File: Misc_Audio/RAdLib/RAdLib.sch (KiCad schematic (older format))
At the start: 45 parts, among them J5 AudioJack3, Q1 2N3904, U1 YM3812, U2 YM3014B, U3 RC4136, U4 LM386, X1 ECS-2100AX-3.579545MHZ

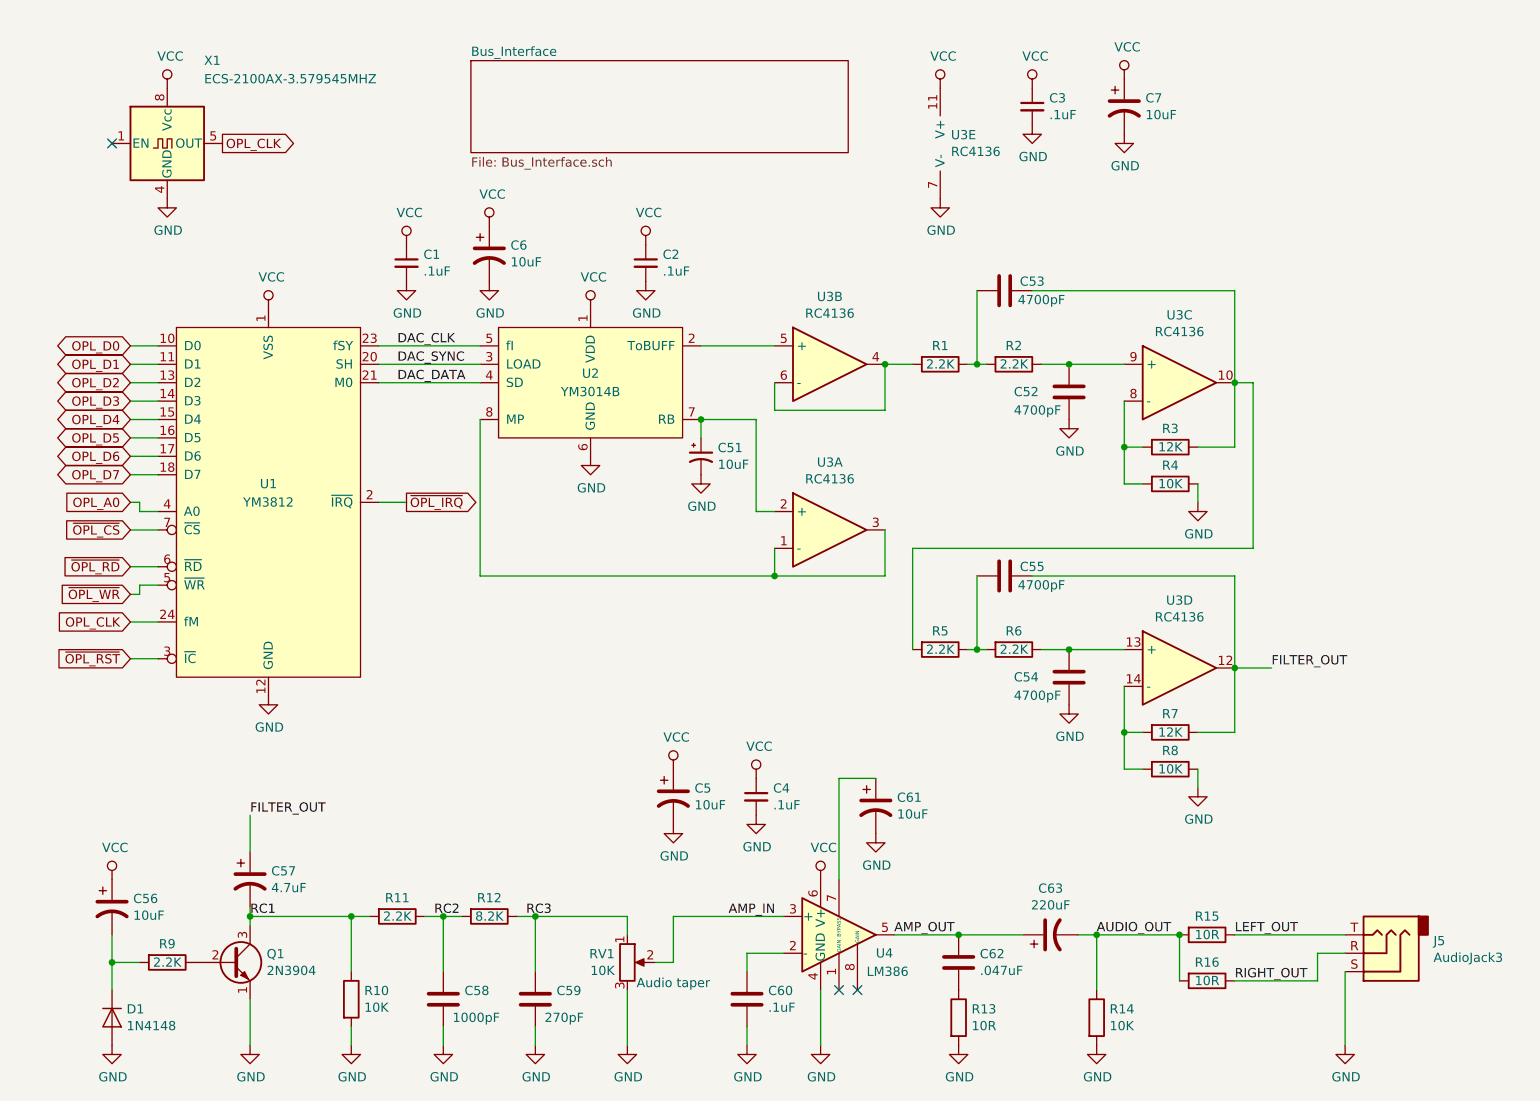
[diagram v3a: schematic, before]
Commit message: Update the active filter stages after the DAC to work with the power supply constraints on the RPI.  Document what needs to be done to the audio output section.
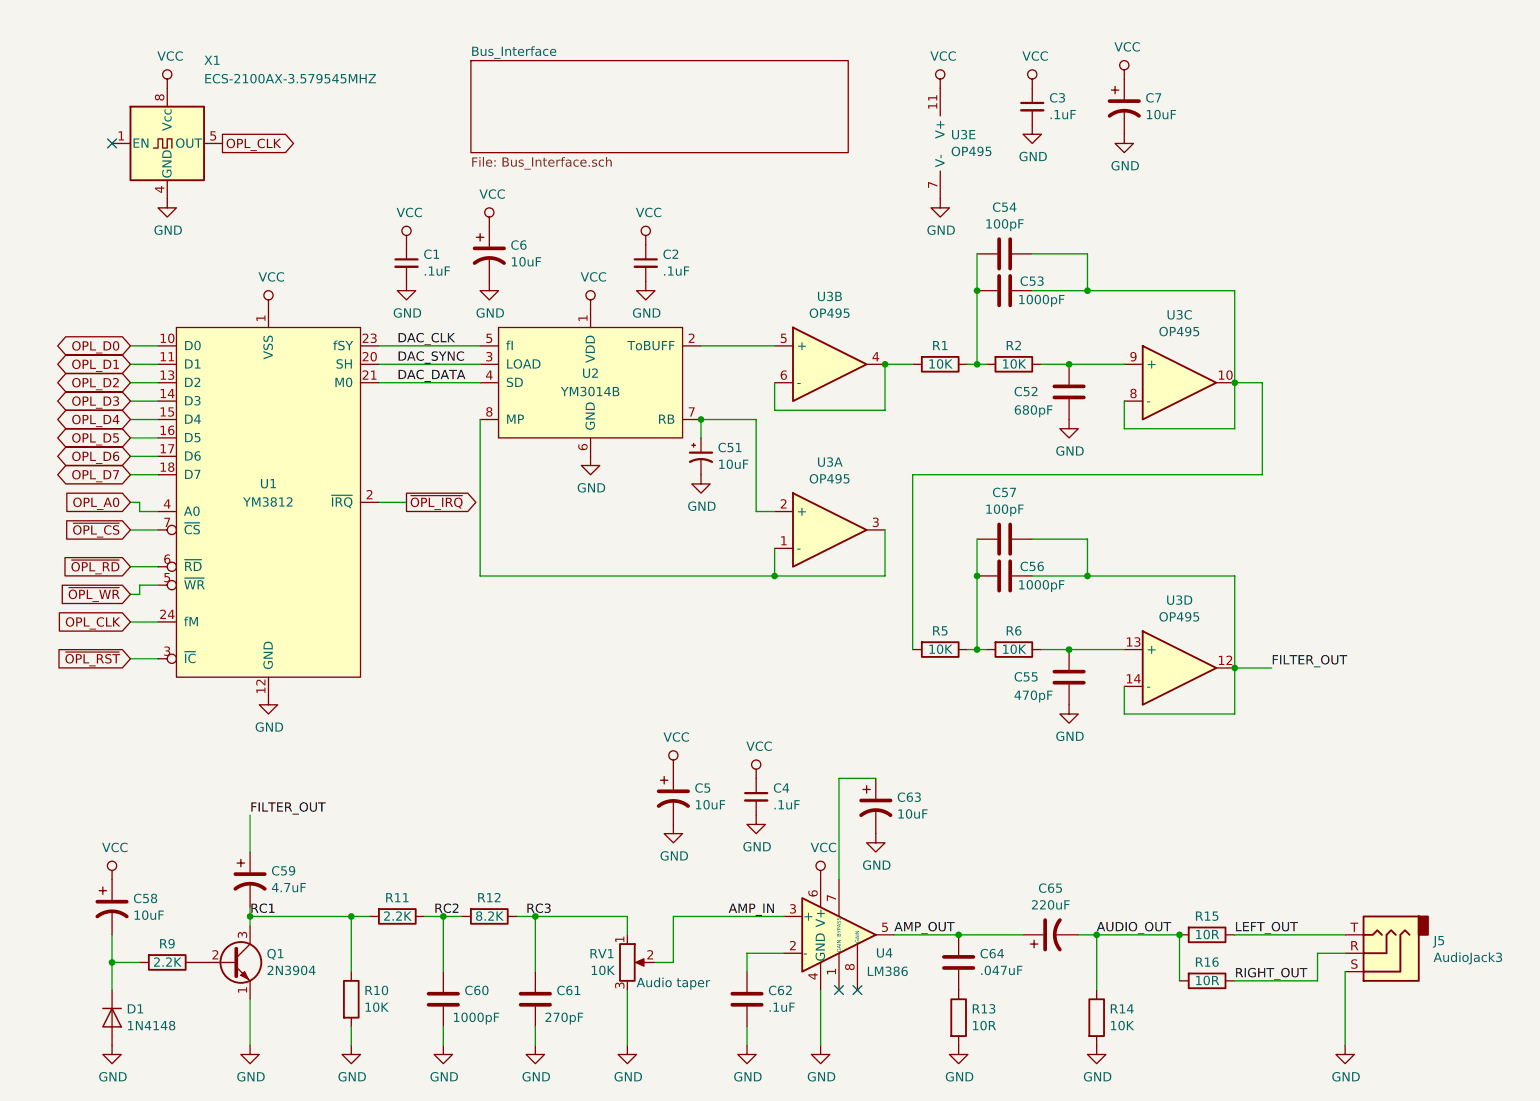
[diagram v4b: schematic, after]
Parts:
- removed R3, R7: 12K, Resistor_THT:R_Axial_DIN0204_L3.6mm_D1.6mm_P5.08mm_Horizontal, symbol Device:R
- removed R4, R8: 10K, Resistor_THT:R_Axial_DIN0204_L3.6mm_D1.6mm_P5.08mm_Horizontal, symbol Device:R
- added C54, C57: 100pF, symbol Device:C
- C52: value 4700pF -> 680pF
- C53: value 4700pF -> 1000pF
- C55: renamed from C54; value 4700pF -> 470pF
- C56: renamed from C55; value 4700pF -> 1000pF
- R1, R2, R5, R6: value 2.2K -> 10K
- U3: value RC4136 -> OP495
- renumbered C56 to C58, C57 to C59, C58 to C60, C59 to C61, C60 to C62, C61 to C63, C62 to C64, C63 to C65
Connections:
- net FILTER_OUT: now also U3.14 (-), C57.1
- net at C53.2, R1.1, R2.2: now also C54.2
- net at C53.1, R5.2, U3.10: now also U3.8 (-), C54.1
- net at C56.2, R5.1, R6.2: now also C57.2

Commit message: Rework the audio output section as an AC-coupled emitter-follower.
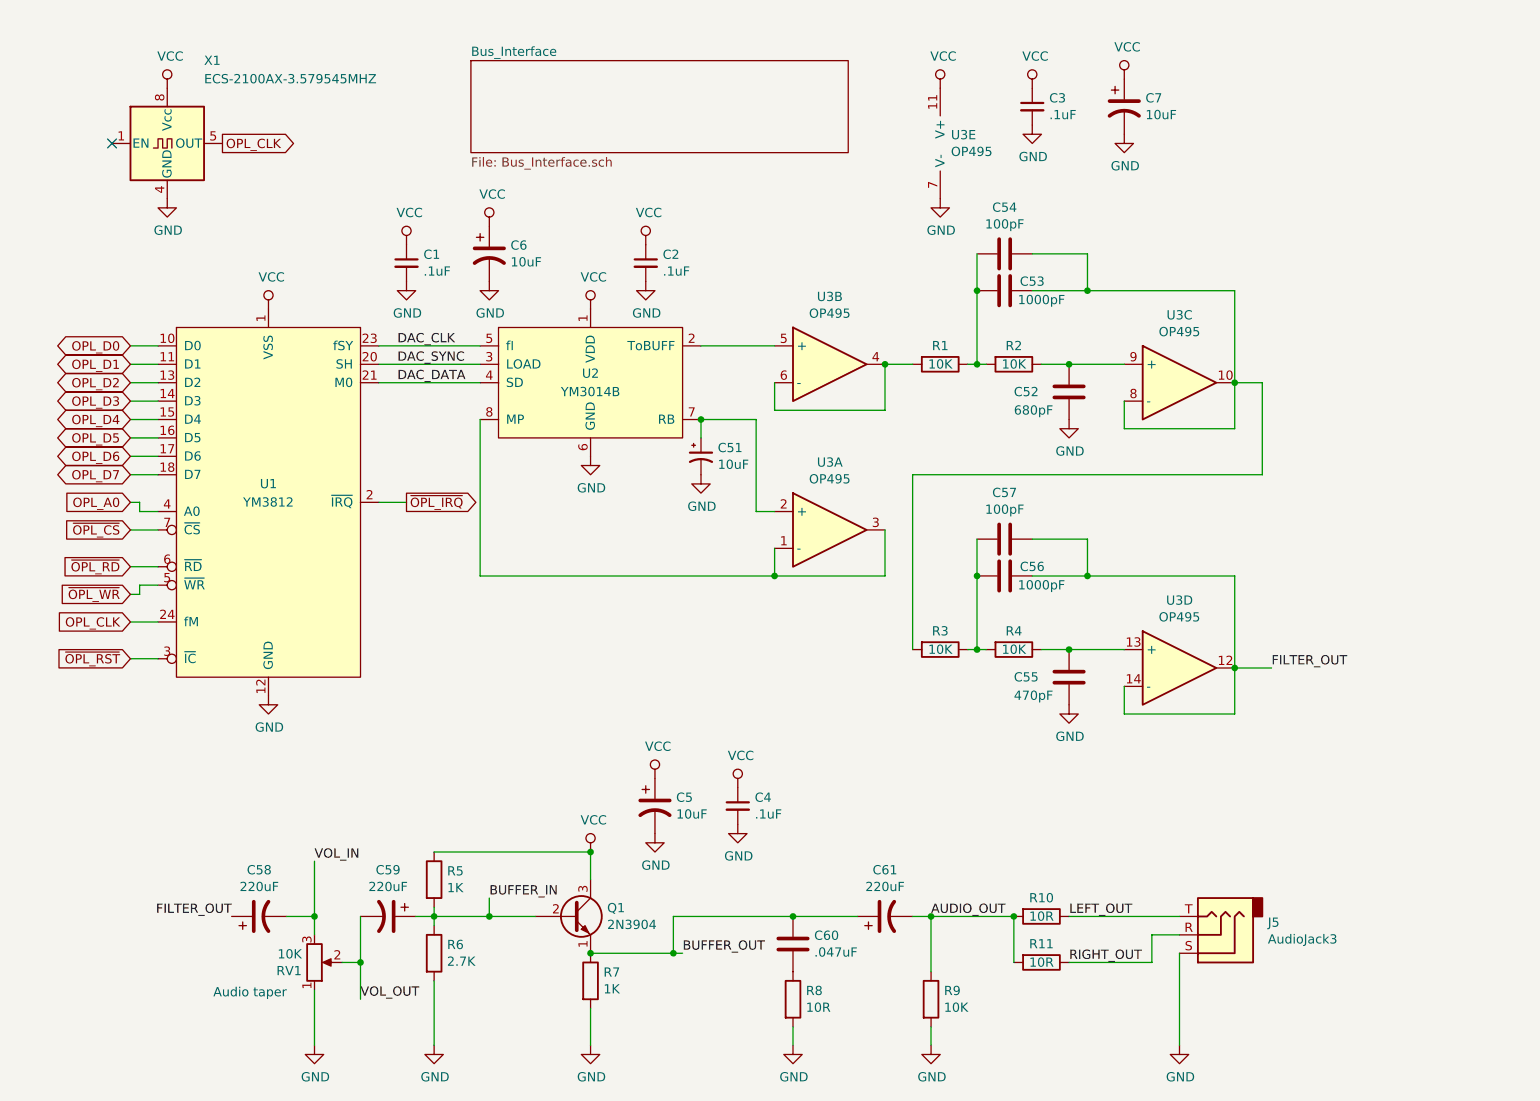
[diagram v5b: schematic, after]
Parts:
- removed C60: 1000pF, Capacitor_THT:C_Disc_D5.0mm_W2.5mm_P2.50mm, symbol Device:C
- removed C61: 270pF, Capacitor_THT:C_Disc_D5.0mm_W2.5mm_P2.50mm, symbol Device:C
- removed C62: .1uF, Capacitor_THT:C_Disc_D5.0mm_W2.5mm_P2.50mm, symbol Device:C
- removed C63: 10uF, Capacitor_THT:CP_Radial_D5.0mm_P2.50mm, symbol Device:CP1
- removed D1: 1N4148, Diode_THT:D_DO-35_SOD27_P7.62mm_Horizontal, symbol Device:D
- removed R10: 10K, Resistor_THT:R_Axial_DIN0204_L3.6mm_D1.6mm_P5.08mm_Horizontal, symbol Device:R
- removed R11, R9: 2.2K, Resistor_THT:R_Axial_DIN0204_L3.6mm_D1.6mm_P5.08mm_Horizontal, symbol Device:R
- removed R12: 8.2K, Resistor_THT:R_Axial_DIN0204_L3.6mm_D1.6mm_P5.08mm_Horizontal, symbol Device:R
- removed U4: LM386, Package_DIP:DIP-8_W7.62mm, symbol Amplifier_Audio:LM386
- added R5, R7: 1K, Resistor_THT:R_Axial_DIN0204_L3.6mm_D1.6mm_P5.08mm_Horizontal, symbol Device:R
- added R6: 2.7K, Resistor_THT:R_Axial_DIN0204_L3.6mm_D1.6mm_P5.08mm_Horizontal, symbol Device:R
- C54, C57: footprint (none) -> Capacitor_THT:C_Disc_D5.0mm_W2.5mm_P2.50mm
- C58: value 10uF -> 220uF; footprint Capacitor_THT:CP_Radial_D5.0mm_P2.50mm -> Capacitor_THT:CP_Axial_L18.0mm_D8.0mm_P25.00mm_Horizontal; Part AVX TAP106K016SCS -> (none)
- C59: value 4.7uF -> 220uF; footprint Capacitor_THT:CP_Radial_D5.0mm_P2.50mm -> Capacitor_THT:CP_Axial_L18.0mm_D8.0mm_P25.00mm_Horizontal; Part AVX TAP475K016SCS -> (none)
- U3: footprint Package_DIP:DIP-14_W7.62mm -> Package_DIP:DIP-14_W7.62mm_Socket
- renumbered C64 to C60, C65 to C61, R15 to R10, R16 to R11, R5 to R3, R6 to R4, R13 to R8, R14 to R9
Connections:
- net RC3 is gone; now on net GND: RV1.1
- net FILTER_OUT: now also C58.1; no longer C59.1
- net GND: now also R6.2, R7.2; no longer Q1.1 (E), RV1.3
- net VCC: now also Q1.3 (C), R5.1; no longer C58.1
- net VOL_IN: now reaches C58.2
- net VOL_IN: now also RV1.3
- net BUFFER_IN: now reaches Q1.2 (B)
- net BUFFER_IN: now also C59.1, R5.2, R6.1
- net AMP_IN renamed VOL_OUT
- net VOL_OUT: now also C59.2
- net AMP_OUT renamed BUFFER_OUT
- net BUFFER_OUT: now also Q1.1 (E), R7.1
- removed net RC1: C59.2, Q1.3 (C)
- no-connect marks 3 -> 1
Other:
- moved on the sheet: C4, C5, C60, C61, J5, Q1, R10, R11, R8, R9, RV1
